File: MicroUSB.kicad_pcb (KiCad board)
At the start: 2 copper layers, 13.5 x 18.8 mm, 11 parts, among them J1 USB_OTG, J2 Conn_01x05, Q1 MMBT3904, U1 USBLC6-2SC6

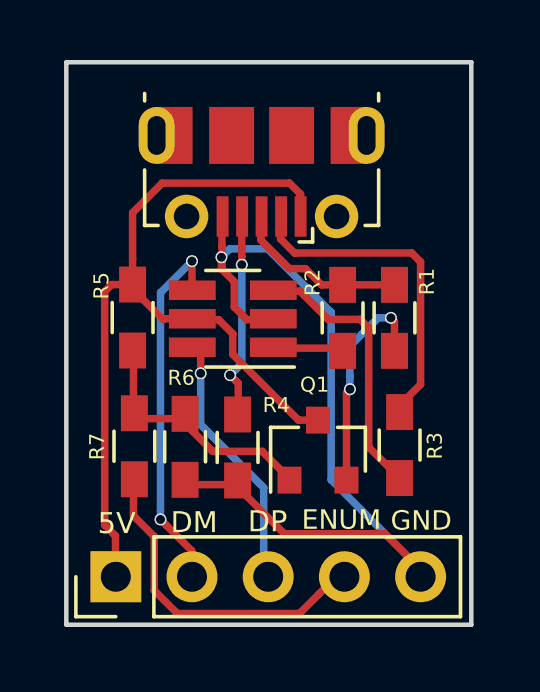
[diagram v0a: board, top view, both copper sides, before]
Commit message: Re-designed (using non-handsolder footprint)
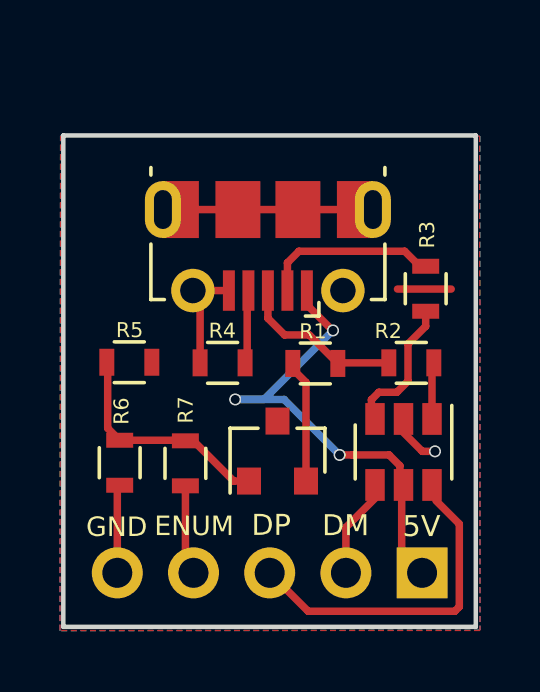
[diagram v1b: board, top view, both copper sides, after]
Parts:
- J2: moved to B.Cu
- R1, R2, R3, R4, R6, R7: footprint Resistors_SMD:R_0603_HandSoldering -> Resistors_SMD:R_0603
- R5: value R -> 10K; footprint Resistors_SMD:R_0603_HandSoldering -> Resistors_SMD:R_0603
- U1: footprint TO_SOT_Packages_SMD:SOT-23-6_Handsoldering -> TO_SOT_Packages_SMD:SOT-23-6
- moved J2 10.2 mm to (157.9, 125.8)
- moved U1 7.22 mm to (157.2, 121.7), turned to 270 degrees
- moved R3 5.28 mm to (158.0, 116.3)
- moved R1 3.05 mm to (154.3, 118.8), turned to 0 degrees
- moved R4 2.86 mm to (151.2, 118.8), turned to 0 degrees
- moved R2 2.74 mm to (157.5, 118.8), turned to 180 degrees
- moved J1 2.48 mm to (152.7, 114.0)
- moved R6 2.24 mm to (147.8, 122.1)
- moved R7 1.79 mm to (150.0, 122.1)
- moved R5 1.49 mm to (148.1, 118.8), turned to 180 degrees
- moved Q1 1.35 mm to (153.0, 121.7)
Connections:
- J1 pad 6: (no net) -> GND
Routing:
- net GND: track 29.4 -> 15.4 mm
- net +5V: track 28.7 -> 17.1 mm, vias 0 -> 3
- net /DM: track 12.2 -> 3.26 mm, vias 2 -> 0
- net /USB_ENUM: track 11.1 -> 4.21 mm
- net Net-(J1-Pad2): track 11.5 -> 5.90 mm
- net Net-(J1-Pad4): track 7.32 -> 2.46 mm, vias 2 -> 0
- net Net-(R3-Pad1): track 8.96 -> 4.83 mm
- net Net-(Q1-Pad2): track 7.44 -> 4.10 mm, vias 2 -> 0
- net /DP: track 8.34 -> 11.0 mm, vias 1 -> 0
- net (no net): track 0.00 -> 1.79 mm
- net Net-(Q1-Pad1): track 8.46 -> 7.48 mm
- net Net-(J1-Pad3): track 6.21 -> 5.60 mm
- added copper zone on F.Cu, net +5V
- removed copper zone on F.Cu, net GND
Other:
- board size 13.5 x 18.8 mm -> 13.8 x 16.4 mm

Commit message: Moved the top edge cut further inwards
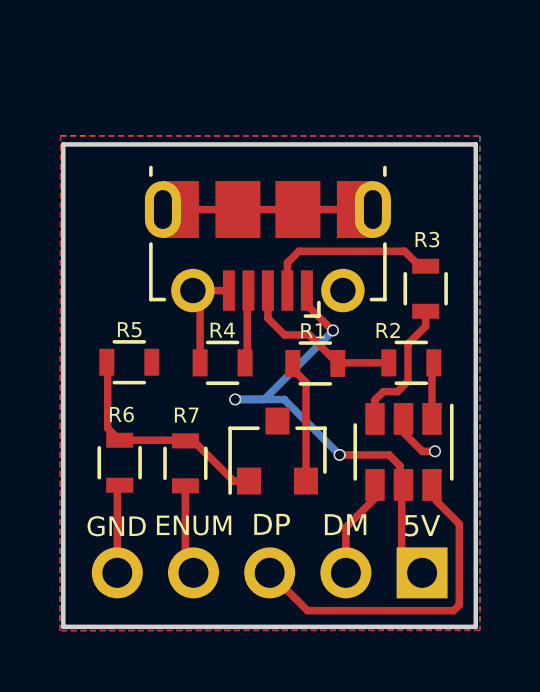
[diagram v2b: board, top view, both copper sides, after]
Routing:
- net (no net): track 1.79 -> 0.00 mm
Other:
- board size 13.8 x 16.4 mm -> 13.8 x 16.1 mm
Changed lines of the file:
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@@
     (links 29)
     (no_connects 0)
-    (area 145.824999 111.114999 159.725001 127.645001)
+    (area 145.824999 111.414999 159.725001 127.645001)
     (thickness 1.6)
     (drawings 25)
-    (tracks 86)
+    (tracks 85)
     (zones 0)
     (modules 11)
@@
     (tags "resistor 0603")
     (attr smd)
-    (fp_text reference R3 (at 1.8 0.05 270) (layer F.SilkS)
+    (fp_text reference R3 (at 1.62 0.05 360) (layer F.SilkS)
       (effects (font (size 0.5 0.5) (thickness 0.125)))
     )
@@
     (tags "resistor 0603")
     (attr smd)
-    (fp_text reference R6 (at 1.72 0.06 90) (layer F.SilkS)
+    (fp_text reference R6 (at 1.59 0.06 180) (layer F.SilkS)
       (effects (font (size 0.5 0.5) (thickness 0.125)))
     )
@@
     (tags "resistor 0603")
     (attr smd)
-    (fp_text reference R7 (at 1.78 0.01 90) (layer F.SilkS)
+    (fp_text reference R7 (at 1.59 0.04 180) (layer F.SilkS)
       (effects (font (size 0.5 0.5) (thickness 0.125)))
     )
@@
     )
   )
-  (gr_line (start 145.9 127.57) (end 145.9 111.19) (layer Edge.Cuts) (width 0.15))
-  (gr_line (start 159.65 127.57) (end 159.65 111.19) (layer Edge.Cuts) (width 0.15))
+  (gr_line (start 145.9 127.57) (end 145.9 111.49) (layer Edge.Cuts) (width 0.15))
+  (gr_line (start 159.65 127.57) (end 159.65 111.49) (layer Edge.Cuts) (width 0.15))
   (gr_line (start 145.9 127.57) (end 159.65 127.57) (layer Edge.Cuts) (width 0.15))
-  (gr_line (start 159.65 111.19) (end 145.9 111.19) (layer Edge.Cuts) (width 0.15))
+  (gr_line (start 159.65 111.49) (end 145.9 111.49) (layer Edge.Cuts) (width 0.15))
   (gr_text Micro_USB_Connector (at 152.82 123.61) (layer B.SilkS)
     (effects (font (size 0.5 0.5) (thickness 0.125)) (justify mirror))
@@
     (effects (font (size 0.7 0.7) (thickness 0.175)))
   )
-  (segment (start 157.04 116.31) (end 158.83 116.31) (width 0.25) (layer F.Cu) (net 0))
   (segment (start 157.865736 121.72) (end 158.29 121.72) (width 0.25) (layer F.Cu) (net 1))
   (segment (start 157.12 120.974264) (end 157.865736 121.72) (width 0.25) (layer F.Cu) (net 1))
@@
   (segment (start 147.7 125.77) (end 147.7 122.93) (width 0.25) (layer F.Cu) (net 1))
   (segment (start 147.7 122.93) (end 147.78 122.85) (width 0.25) (layer F.Cu) (net 1))
-  (segment (start 151.19 113.54) (end 151.159998 113.570002) (width 0.25) (layer F.Cu) (net 1))
   (segment (start 153.37 116.36) (end 153.37 115.435) (width 0.25) (layer F.Cu) (net 2))
   (segment (start 153.37 115.435) (end 153.755 115.05) (width 0.25) (layer F.Cu) (net 2))
@@
   (segment (start 157.28 115.05) (end 157.78 115.55) (width 0.25) (layer F.Cu) (net 2))
   (segment (start 157.78 115.55) (end 157.98 115.55) (width 0.25) (layer F.Cu) (net 2))
-  (segment (start 151.63 119.99) (end 152.590004 119.99) (width 0.25) (layer B.Cu) (net 3))
-  (segment (start 152.590004 119.99) (end 154.89 117.690004) (width 0.25) (layer B.Cu) (net 3))
+  (segment (start 154.89 117.690004) (end 154.89 117.7) (width 0.25) (layer B.Cu) (net 3))
+  (segment (start 154.89 117.7) (end 152.6 119.99) (width 0.25) (layer B.Cu) (net 3))
+  (segment (start 152.6 119.99) (end 151.63 119.99) (width 0.25) (layer B.Cu) (net 3))
   (segment (start 155.11 121.84) (end 153.26 119.99) (width 0.25) (layer B.Cu) (net 3))
   (segment (start 153.26 119.99) (end 151.63 119.99) (width 0.25) (layer B.Cu) (net 3))
@@
   (segment (start 155.32 124.255) (end 156.41 123.165) (width 0.25) (layer F.Cu) (net 6))
   (segment (start 156.41 123.165) (end 156.41 122.96) (width 0.25) (layer F.Cu) (net 6))
-  (segment (start 152.78 125.77) (end 154.06 127.05) (width 0.25) (layer F.Cu) (net 7))
+  (segment (start 152.78 125.77) (end 154.04 127.03) (width 0.25) (layer F.Cu) (net 7))
+  (segment (start 154.04 127.03) (end 158.91 127.03) (width 0.25) (layer F.Cu) (net 7))
+  (segment (start 158.91 127.03) (end 159.1 126.84) (width 0.25) (layer F.Cu) (net 7))
+  (segment (start 159.1 126.84) (end 159.1 124.14) (width 0.25) (layer F.Cu) (net 7))
   (segment (start 159.1 124.14) (end 158.32 123.36) (width 0.25) (layer F.Cu) (net 7))
-  (segment (start 154.06 127.05) (end 158.95 127.05) (width 0.25) (layer F.Cu) (net 7))
-  (segment (start 158.95 127.05) (end 159.1 126.9) (width 0.25) (layer F.Cu) (net 7))
-  (segment (start 159.1 126.9) (end 159.1 124.14) (width 0.25) (layer F.Cu) (net 7))
   (segment (start 152.72 125.64) (end 152.58 125.5) (width 0.25) (layer B.Cu) (net 7))
   (segment (start 149.97 122.87) (end 149.97 125.5) (width 0.25) (layer F.Cu) (net 8))
@@
   (segment (start 157.98 117.55) (end 157.39 118.14) (width 0.25) (layer F.Cu) (net 12))
   (segment (start 157.39 118.14) (end 157.39 119.38) (width 0.25) (layer F.Cu) (net 12))
-  (segment (start 157.02 119.75) (end 156.42 119.75) (width 0.25) (layer F.Cu) (net 12))
-  (segment (start 157.39 119.38) (end 157.02 119.75) (width 0.25) (layer F.Cu) (net 12))
-  (segment (start 156.42 119.75) (end 156.17 120) (width 0.25) (layer F.Cu) (net 12))
-  (segment (start 156.17 120) (end 156.17 120.78) (width 0.25) (layer F.Cu) (net 12))
+  (segment (start 157.39 119.38) (end 157.04 119.73) (width 0.25) (layer F.Cu) (net 12))
+  (segment (start 156.57 119.73) (end 156.29 120.01) (width 0.25) (layer F.Cu) (net 12))
+  (segment (start 157.04 119.73) (end 156.57 119.73) (width 0.25) (layer F.Cu) (net 12))
+  (segment (start 156.29 120.01) (end 156.29 120.64) (width 0.25) (layer F.Cu) (net 12))
   (zone (net 3) (net_name +5V) (layer F.Cu) (hatch edge 0.508)
     (connect_pads (clearance 0.508))

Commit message: Changed the size of text to 0.8x1.0 mm
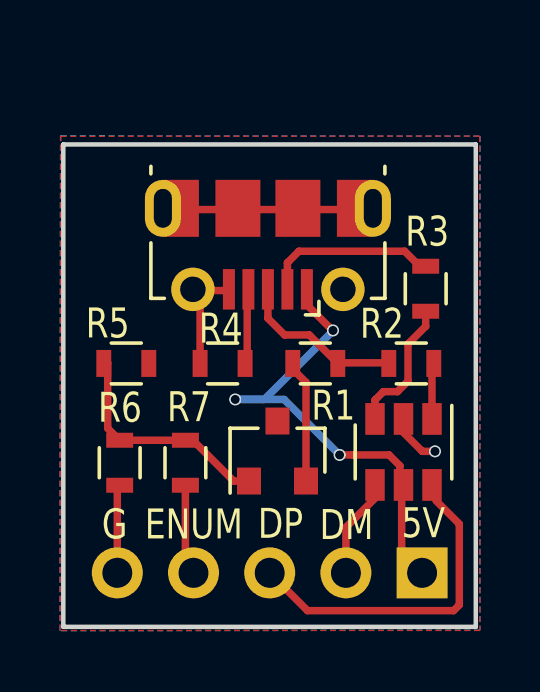
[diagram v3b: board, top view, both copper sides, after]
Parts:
- moved R5 0.11 mm to (148.0, 118.8)
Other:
- board text added: "G"
- board text removed: "GND"
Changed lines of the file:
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@@
   )
   (module Connectors_USB:USB_Micro-B_Molex-105017-0001 (layer F.Cu)
-    (at 152.72 114.01 180)
+    (at 152.72 113.97 180)
     (descr http://www.molex.com/pdm_docs/sd/1050170001_sd.pdf)
     (tags "Micro-USB SMD Typ-B")
@@
   )
   (module Resistors_SMD:R_0603 (layer F.Cu)
-    (at 157.5 118.77 180)
-    (descr "Resistor SMD 0603, reflow soldering, Vishay (see dcrcw.pdf)")
-    (tags "resistor 0603")
-    (attr smd)
-    (fp_text reference R2 (at 0.77 1.06 180) (layer F.SilkS)
-      (effects (font (size 0.5 0.5) (thickness 0.125)))
+    (at 157.5 118.79 180)
+    (descr "Resistor SMD 0603, reflow soldering, Vishay (see dcrcw.pdf)")
+    (tags "resistor 0603")
+    (attr smd)
+    (fp_text reference R2 (at 0.98 1.32 180) (layer F.SilkS)
+      (effects (font (size 1 0.8) (thickness 0.2)))
     )
     (fp_text value 20R (at 0 1.5 180) (layer F.Fab)
@@
     (tags "resistor 0603")
     (attr smd)
-    (fp_text reference R1 (at -0.08 -1.07) (layer F.SilkS)
-      (effects (font (size 0.5 0.5) (thickness 0.125)))
+    (fp_text reference R1 (at 0.6 1.41 180) (layer F.SilkS)
+      (effects (font (size 1 0.8) (thickness 0.2)))
     )
     (fp_text value 1k5 (at 0 1.5) (layer F.Fab)
@@
     (tags "resistor 0603")
     (attr smd)
-    (fp_text reference R3 (at 1.62 0.05 360) (layer F.SilkS)
-      (effects (font (size 0.5 0.5) (thickness 0.125)))
+    (fp_text reference R3 (at 1.9 0.05 180) (layer F.SilkS)
+      (effects (font (size 1 0.8) (thickness 0.2)))
     )
     (fp_text value 20R (at 0 1.5 90) (layer F.Fab)
@@
   )
   (module Resistors_SMD:R_0603 (layer F.Cu)
-    (at 151.21 118.77)
-    (descr "Resistor SMD 0603, reflow soldering, Vishay (see dcrcw.pdf)")
-    (tags "resistor 0603")
-    (attr smd)
-    (fp_text reference R4 (at -0.01 -1.07) (layer F.SilkS)
-      (effects (font (size 0.5 0.5) (thickness 0.125)))
+    (at 151.21 118.79)
+    (descr "Resistor SMD 0603, reflow soldering, Vishay (see dcrcw.pdf)")
+    (tags "resistor 0603")
+    (attr smd)
+    (fp_text reference R4 (at -0.06 -1.16 180) (layer F.SilkS)
+      (effects (font (size 1 0.8) (thickness 0.2)))
     )
     (fp_text value 100k (at 0 1.5) (layer F.Fab)
@@
   )
   (module Resistors_SMD:R_0603 (layer F.Cu)
-    (at 148.1 118.75 180)
-    (descr "Resistor SMD 0603, reflow soldering, Vishay (see dcrcw.pdf)")
-    (tags "resistor 0603")
-    (attr smd)
-    (fp_text reference R5 (at -0.01 1.07 180) (layer F.SilkS)
-      (effects (font (size 0.5 0.5) (thickness 0.125)))
+    (at 148 118.79 180)
+    (descr "Resistor SMD 0603, reflow soldering, Vishay (see dcrcw.pdf)")
+    (tags "resistor 0603")
+    (attr smd)
+    (fp_text reference R5 (at 0.62 1.33 360) (layer F.SilkS)
+      (effects (font (size 1 0.8) (thickness 0.2)))
     )
     (fp_text value 10K (at 0 1.5 180) (layer F.Fab)
@@
     (tags "resistor 0603")
     (attr smd)
-    (fp_text reference R6 (at 1.59 0.06 180) (layer F.SilkS)
-      (effects (font (size 0.5 0.5) (thickness 0.125)))
+    (fp_text reference R6 (at 1.83 0.01 180) (layer F.SilkS)
+      (effects (font (size 1 0.8) (thickness 0.2)))
     )
     (fp_text value 36k (at 0 1.5 90) (layer F.Fab)
@@
   )
   (module Resistors_SMD:R_0603 (layer F.Cu)
-    (at 149.97 122.12 90)
-    (descr "Resistor SMD 0603, reflow soldering, Vishay (see dcrcw.pdf)")
-    (tags "resistor 0603")
-    (attr smd)
-    (fp_text reference R7 (at 1.59 0.04 180) (layer F.SilkS)
-      (effects (font (size 0.5 0.5) (thickness 0.125)))
+    (at 149.97 122.1 90)
+    (descr "Resistor SMD 0603, reflow soldering, Vishay (see dcrcw.pdf)")
+    (tags "resistor 0603")
+    (attr smd)
+    (fp_text reference R7 (at 1.85 0.12 180) (layer F.SilkS)
+      (effects (font (size 1 0.8) (thickness 0.2)))
     )
     (fp_text value 100R (at 0 1.5 90) (layer F.Fab)
@@
   (gr_line (start 153.4 120.85) (end 154.2 120.47) (layer B.SilkS) (width 0.2))
   (gr_circle (center 152.68 121.91) (end 153.68 121.16) (layer B.SilkS) (width 0.2))
-  (gr_text GND (at 147.68 124.24) (layer F.SilkS)
-    (effects (font (size 0.65 0.65) (thickness 0.1625)))
-  )
-  (gr_text ENUM (at 150.26 124.21) (layer F.SilkS)
-    (effects (font (size 0.65 0.65) (thickness 0.1625)))
-  )
-  (gr_text DP (at 152.83 124.18) (layer F.SilkS)
-    (effects (font (size 0.7 0.7) (thickness 0.175)))
-  )
-  (gr_text DM (at 155.31 124.19) (layer F.SilkS)
-    (effects (font (size 0.7 0.7) (thickness 0.175)))
-  )
-  (gr_text 5V (at 157.84 124.22) (layer F.SilkS)
-    (effects (font (size 0.7 0.7) (thickness 0.175)))
+  (gr_text G (at 147.61 124.16) (layer F.SilkS)
+    (effects (font (size 1 0.8) (thickness 0.2)))
+  )
+  (gr_text ENUM (at 150.25 124.16) (layer F.SilkS)
+    (effects (font (size 1 0.8) (thickness 0.2)))
+  )
+  (gr_text DP (at 153.14 124.14) (layer F.SilkS)
+    (effects (font (size 1 0.8) (thickness 0.2)))
+  )
+  (gr_text DM (at 155.34 124.18) (layer F.SilkS)
+    (effects (font (size 1 0.8) (thickness 0.2)))
+  )
+  (gr_text 5V (at 157.9 124.12) (layer F.SilkS)
+    (effects (font (size 1 0.8) (thickness 0.2)))
   )
   (segment (start 157.865736 121.72) (end 158.29 121.72) (width 0.25) (layer F.Cu) (net 1))

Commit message: Added dimension and changed DM/DP label to D+/D-
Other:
- board text added: "D+"
- board text added: "D-"
- board text removed: "DM"
- board text removed: "DP"
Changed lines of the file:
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@@
     (links 29)
     (no_connects 0)
-    (area 145.824999 111.414999 159.725001 127.645001)
+    (area 145.684999 109.545 160.555 127.795001)
     (thickness 1.6)
-    (drawings 25)
+    (drawings 27)
     (tracks 85)
     (zones 0)
@@
     )
   )
+  (dimension 16.08 (width 0.3) (layer Eco1.User)
+    (gr_text "16.080 mm" (at 143.2 119.53 270) (layer Eco1.User)
+      (effects (font (size 1.5 1.5) (thickness 0.3)))
+    )
+    (feature1 (pts (xy 145.9 127.57) (xy 141.85 127.57)))
+    (feature2 (pts (xy 145.9 111.49) (xy 141.85 111.49)))
+    (crossbar (pts (xy 144.55 111.49) (xy 144.55 127.57)))
+    (arrow1a (pts (xy 144.55 127.57) (xy 143.963579 126.443496)))
+    (arrow1b (pts (xy 144.55 127.57) (xy 145.136421 126.443496)))
+    (arrow2a (pts (xy 144.55 111.49) (xy 143.963579 112.616504)))
+    (arrow2b (pts (xy 144.55 111.49) (xy 145.136421 112.616504)))
+  )
+  (dimension 13.75 (width 0.3) (layer Eco1.User)
+    (gr_text "13.750 mm" (at 152.775 108.39) (layer Eco1.User)
+      (effects (font (size 1.5 1.5) (thickness 0.3)))
+    )
+    (feature1 (pts (xy 159.65 111.5) (xy 159.65 107.04)))
+    (feature2 (pts (xy 145.9 111.5) (xy 145.9 107.04)))
+    (crossbar (pts (xy 145.9 109.74) (xy 159.65 109.74)))
+    (arrow1a (pts (xy 159.65 109.74) (xy 158.523496 110.326421)))
+    (arrow1b (pts (xy 159.65 109.74) (xy 158.523496 109.153579)))
+    (arrow2a (pts (xy 145.9 109.74) (xy 147.026504 110.326421)))
+    (arrow2b (pts (xy 145.9 109.74) (xy 147.026504 109.153579)))
+  )
   (gr_line (start 145.9 127.57) (end 145.9 111.49) (layer Edge.Cuts) (width 0.15))
   (gr_line (start 159.65 127.57) (end 159.65 111.49) (layer Edge.Cuts) (width 0.15))
@@
     (effects (font (size 1 0.8) (thickness 0.2)))
   )
-  (gr_text DP (at 153.14 124.14) (layer F.SilkS)
+  (gr_text D+ (at 153.14 124.14) (layer F.SilkS)
     (effects (font (size 1 0.8) (thickness 0.2)))
   )
-  (gr_text DM (at 155.34 124.18) (layer F.SilkS)
+  (gr_text D- (at 155.34 124.18) (layer F.SilkS)
     (effects (font (size 1 0.8) (thickness 0.2)))
   )
